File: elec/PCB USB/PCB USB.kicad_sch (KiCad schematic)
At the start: 3 parts

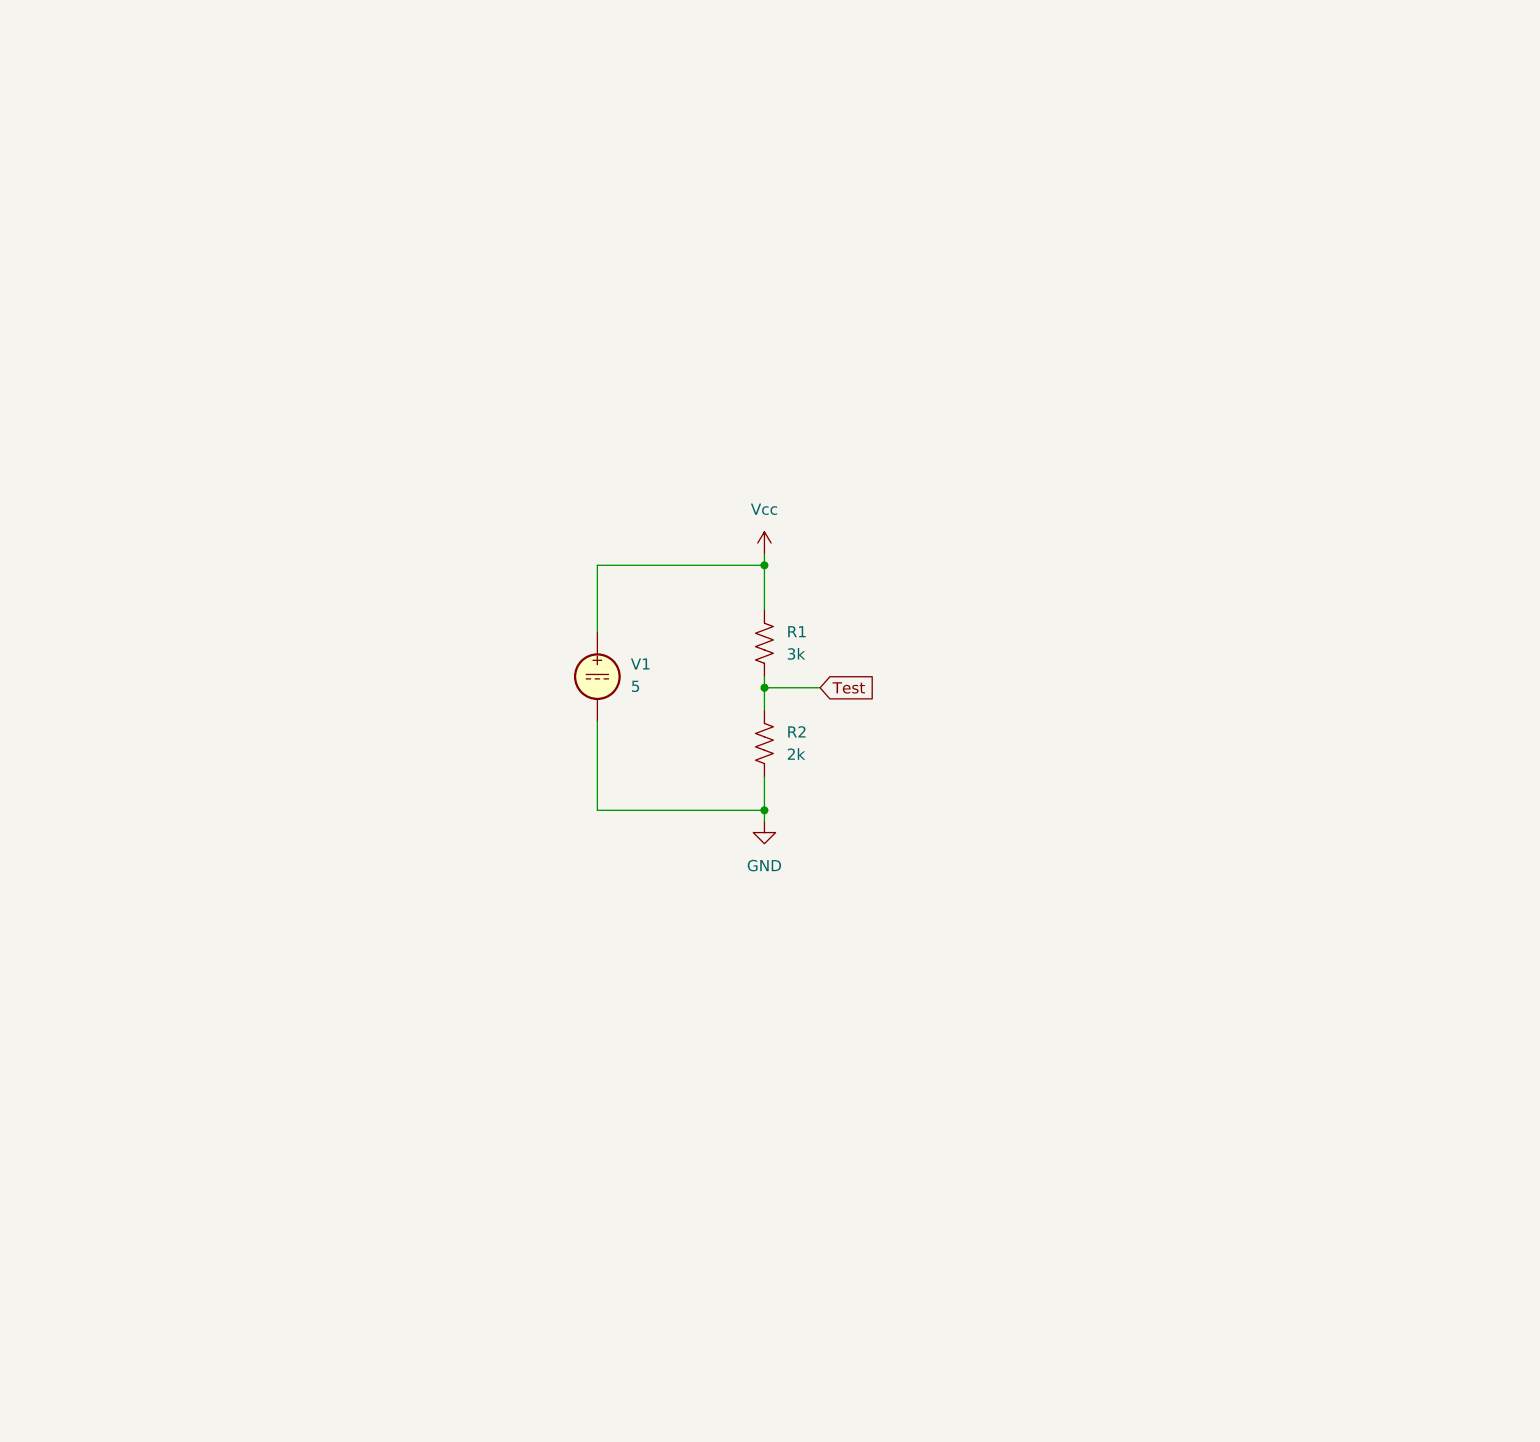
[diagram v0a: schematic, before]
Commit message: push rp2350, USB hub, power. SCHEMATIC
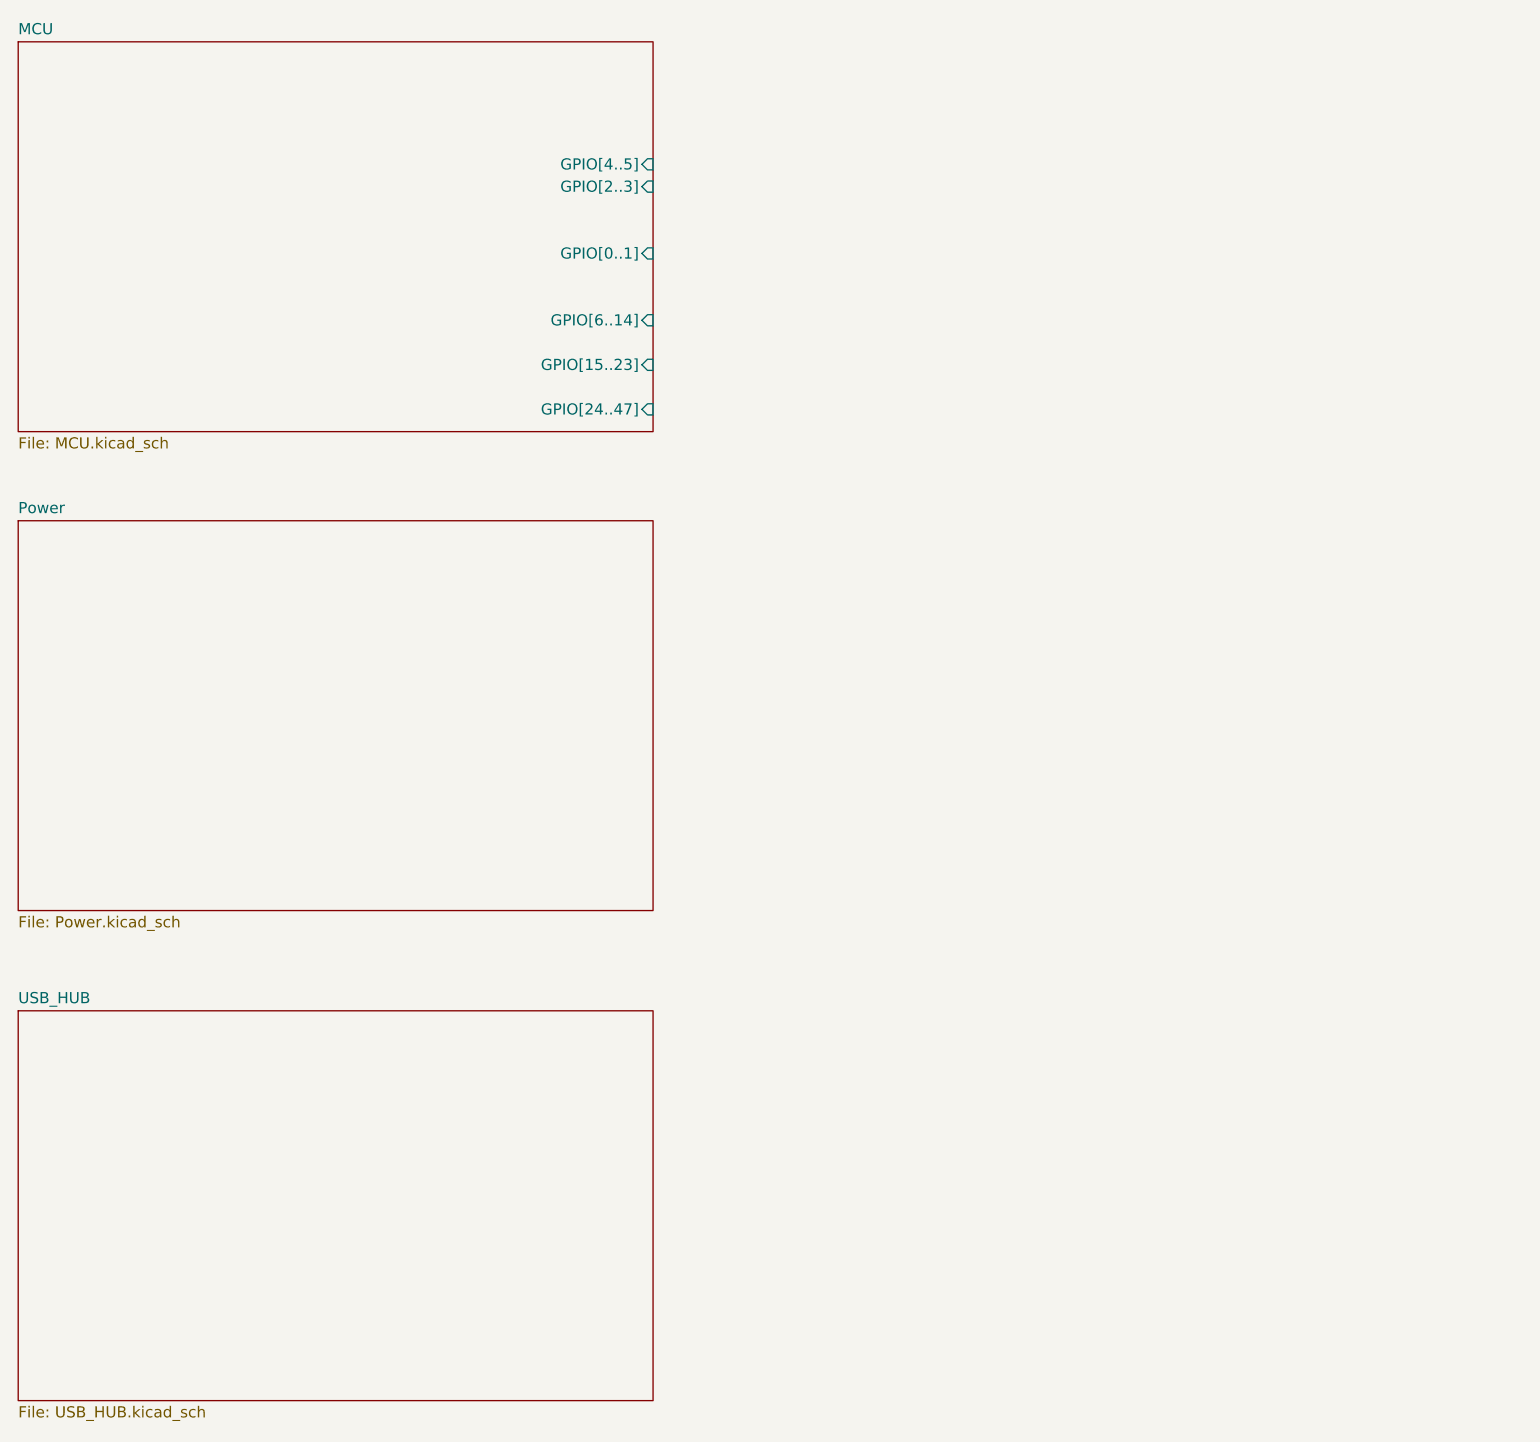
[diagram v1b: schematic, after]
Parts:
- removed R1: 3k, symbol Device:R_US
- removed R2: 2k, symbol Device:R_US
- removed V1: 5, symbol Simulation_SPICE:VDC
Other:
- added sheet MCU (MCU.kicad_sch)
- added sheet Power (Power.kicad_sch)
- added sheet USB_HUB (USB_HUB.kicad_sch)

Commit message: push schema
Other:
- added sheet Output_Input (Output_Input.kicad_sch)
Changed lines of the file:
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@@
+	)
+	(sheet
+		(at 114.3 19.05)
+		(size 73.66 44.45)
+		(exclude_from_sim no)
+		(in_bom yes)
+		(on_board yes)
+		(dnp no)
+		(fields_autoplaced yes)
+		(stroke
+			(width 0.1524)
+			(type solid)
+		)
+		(fill
+			(color 0 0 0 0.0000)
+		)
+		(property "Sheetname" "Output_Input"
+			(at 114.3 18.3384 0)
+			(effects
+				(font
+					(size 1.27 1.27)
+				)
+				(justify left bottom)
+			)
+		)
+		(property "Sheetfile" "Output_Input.kicad_sch"
+			(at 114.3 64.0846 0)
+			(effects
+				(font
+					(size 1.27 1.27)
+				)
+				(justify left top)
+			)
+		)
+		(instances
+			(project "PCB USB"
+				(path "/3ce8e8a6-ebd4-4bdc-aa1f-eee2b03be2d2"
+					(page "5")
+				)
+			)
+		)
 	)
 	(sheet

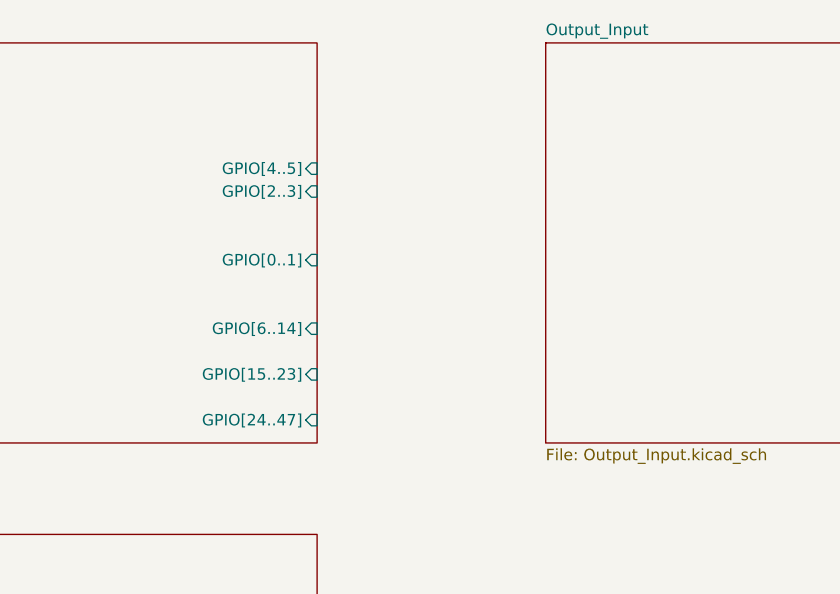
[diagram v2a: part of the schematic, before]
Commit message: push sélection pièces et schéma électrique clean up
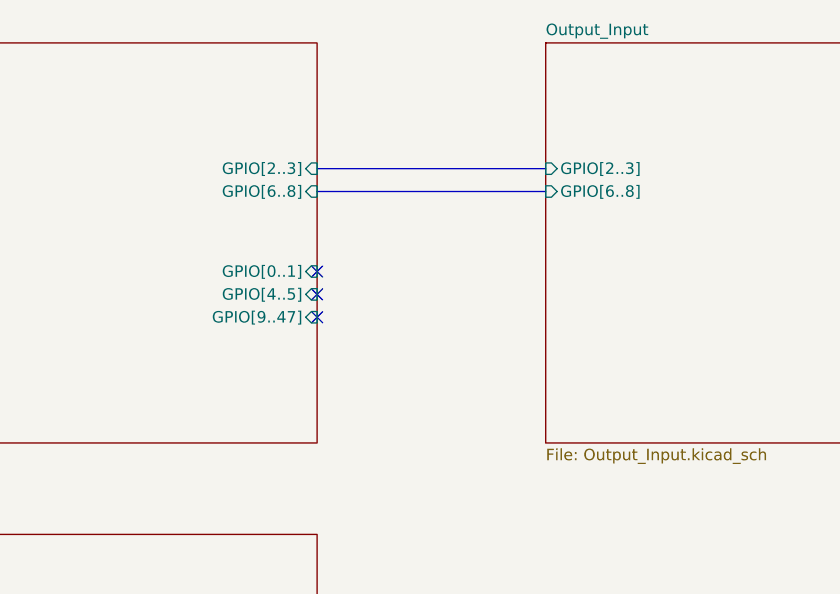
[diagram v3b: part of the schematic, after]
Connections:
- no-connect marks 0 -> 3
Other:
- sheet MCU ports: added GPIO[6..8], GPIO[9..47]; removed GPIO[15..23], GPIO[24..47], GPIO[6..14]
- sheet Output_Input ports: added GPIO[2..3], GPIO[6..8]; removed none
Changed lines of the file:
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@@
 		(comment 4 "By : Charles-Ariel Dion")
+	)
+	(no_connect
+		(at 88.9 49.53)
+	)
+	(no_connect
+		(at 88.9 44.45)
+	)
+	(no_connect
+		(at 88.9 46.99)
+	)
+	(bus
+		(pts
+			(xy 88.9 33.02) (xy 114.3 33.02)
+		)
+		(stroke
+			(width 0)
+			(type default)
+		)
+	)
+	(bus
+		(pts
+			(xy 88.9 35.56) (xy 114.3 35.56)
+		)
+		(stroke
+			(width 0)
+			(type default)
+		)
 	)
 	(sheet
@@
 				)
 				(justify left top)
+			)
+		)
+		(pin "GPIO[2..3]" input
+			(at 114.3 33.02 180)
+			(effects
+				(font
+					(size 1.27 1.27)
+				)
+				(justify left)
+			)
+		)
+		(pin "GPIO[6..8]" input
+			(at 114.3 35.56 180)
+			(effects
+				(font
+					(size 1.27 1.27)
+				)
+				(justify left)
 			)
 		)
@@
 			)
 		)
-		(pin "GPIO[4..5]" input
+		(pin "GPIO[6..8]" input
+			(at 88.9 35.56 0)
+			(effects
+				(font
+					(size 1.27 1.27)
+				)
+				(justify right)
+			)
+		)
+		(pin "GPIO[9..47]" input
+			(at 88.9 49.53 0)
+			(effects
+				(font
+					(size 1.27 1.27)
+				)
+				(justify right)
+			)
+		)
+		(pin "GPIO[0..1]" input
+			(at 88.9 44.45 0)
+			(effects
+				(font
+					(size 1.27 1.27)
+				)
+				(justify right)
+			)
+		)
+		(pin "GPIO[2..3]" input
 			(at 88.9 33.02 0)
 			(effects
@@
 			)
 		)
-		(pin "GPIO[6..14]" input
-			(at 88.9 50.8 0)
+		(pin "GPIO[4..5]" input
+			(at 88.9 46.99 0)
 			(effects
 				(font
-					(size 1.27 1.27)
-				)
-				(justify right)
-			)
-		)
-		(pin "GPIO[15..23]" input
-			(at 88.9 55.88 0)
-			(effects
-				(font
-					(size 1.27 1.27)
-				)
-				(justify right)
-			)
-		)
-		(pin "GPIO[24..47]" input
-			(at 88.9 60.96 0)
-			(effects
-				(font
-					(size 1.27 1.27)
-				)
-				(justify right)
-			)
-		)
-		(pin "GPIO[0..1]" input
-			(at 88.9 43.18 0)
-			(effects
-				(font
-					(size 1.27 1.27)
-				)
-				(justify right)
-			)
-		)
-		(pin "GPIO[2..3]" input
-			(at 88.9 35.56 0)
-			(effects
-				(font

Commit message: Push non terminé
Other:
- company: (none) -> C3I
- title: Exploration de Kicad :P -> Hub USB2.0 Pomodoro
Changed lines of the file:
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@@
 	(paper "A4")
 	(title_block
-		(title "Exploration de Kicad :P")
-		(date "2025-03-10")
+		(title "Hub USB2.0 Pomodoro")
+		(date "2025-04-20")
 		(rev "1.0")
-		(comment 4 "By : Charles-Ariel Dion")
+		(company "C3I")
+		(comment 1 "Jacob Turcotte")
+		(comment 2 "&")
+		(comment 3 "Charles-Ariel Dion")
+		(comment 4 "Par: Équipe 3")
 	)
 	(no_connect
